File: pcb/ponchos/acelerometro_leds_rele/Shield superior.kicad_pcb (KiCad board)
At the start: 2 copper layers, 55 x 57 mm, 13 parts, among them J1 CONN_01X08, J2 CONN_01X06, J3 CONN_01X10, J4 CONN_01X08, J5 CONN_01X03, J6 Screw_Terminal_1x03, J7 CONN_01X08, K1 AZ850-x, Q1 BC548, U1 7805

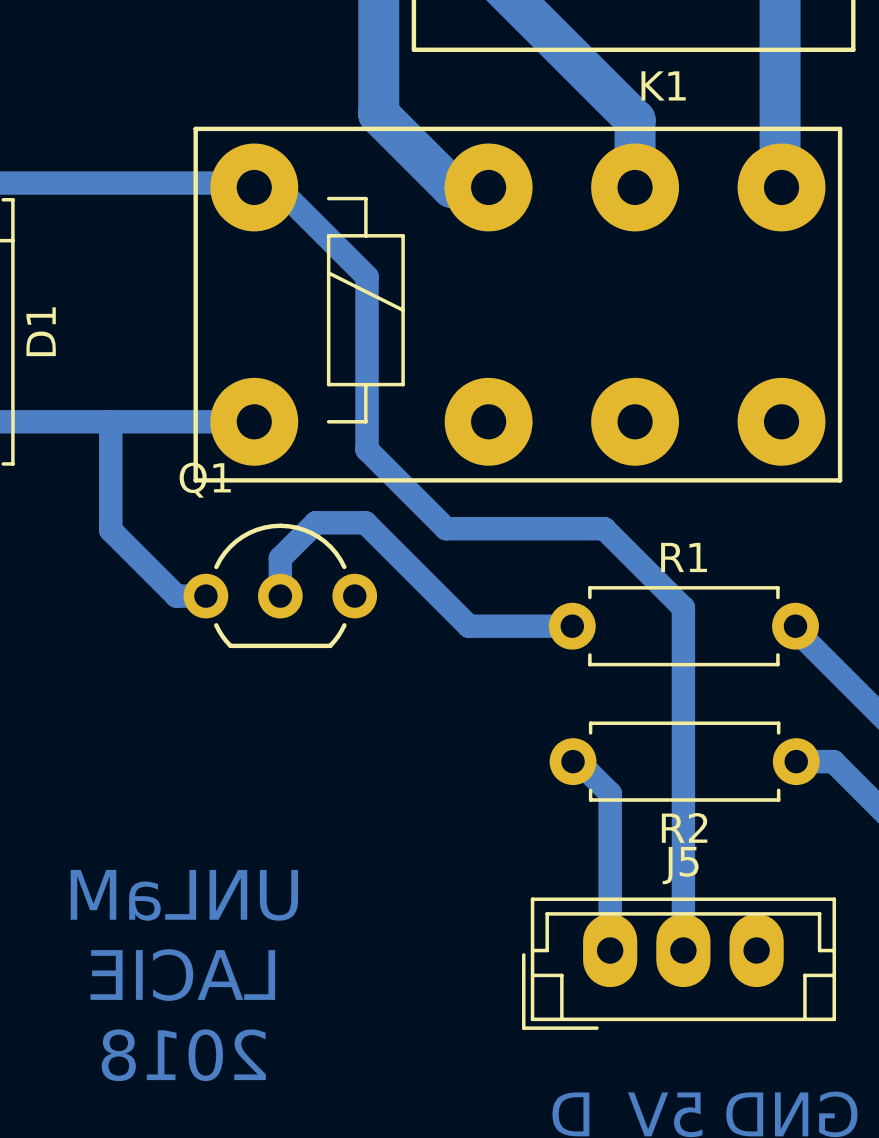
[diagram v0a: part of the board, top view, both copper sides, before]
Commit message: Pads mas grandes para el transistor.
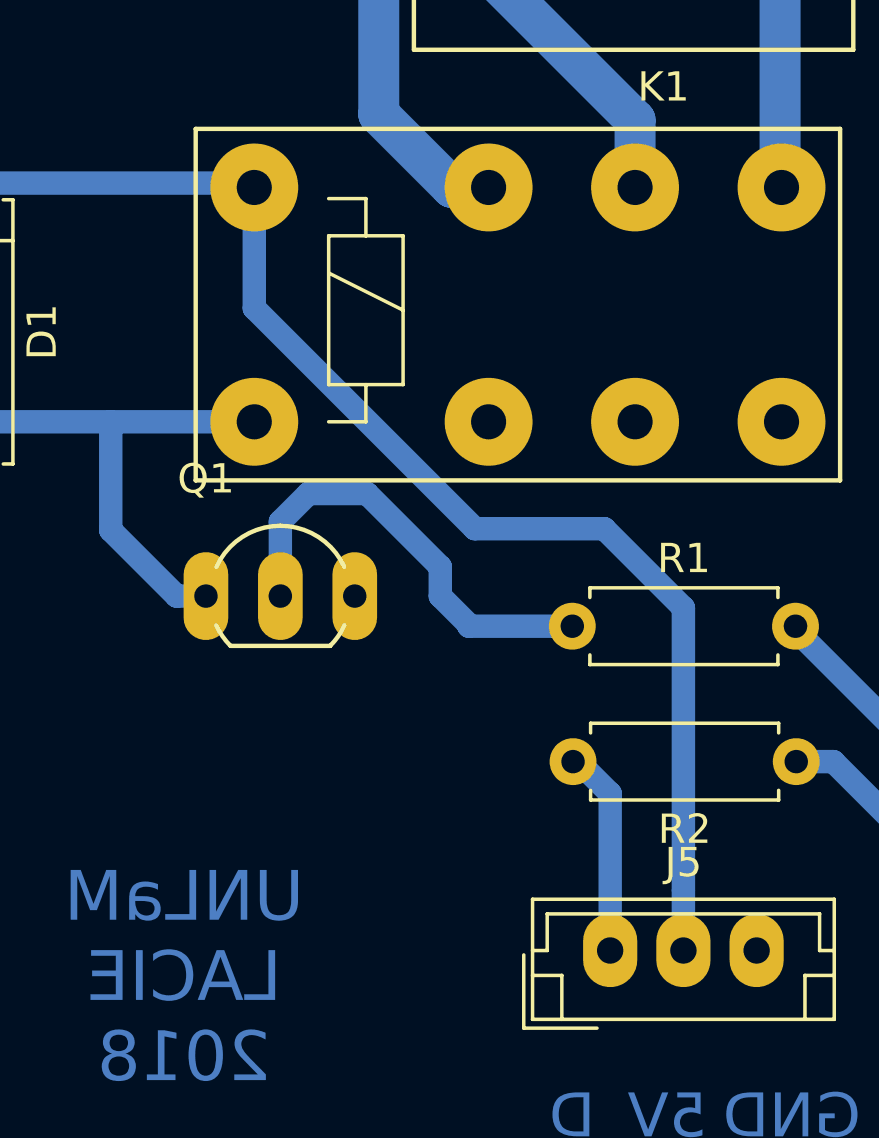
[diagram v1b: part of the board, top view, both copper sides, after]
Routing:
- net Net-(Q1-Pad2): track 13.2 -> 16.7 mm
- net +5V: track 82.6 -> 81.5 mm
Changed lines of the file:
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@@
     (links 21)
     (no_connects 0)
-    (area 20.424999 20.924999 75.575001 78.075001)
+    (area 8.22143 12.8 77.260001 79.900001)
     (thickness 1.6)
     (drawings 12)
-    (tracks 78)
+    (tracks 81)
     (zones 0)
     (modules 13)
@@
   )
   (setup
-    (last_trace_width 0.25)
+    (last_trace_width 0.8)
     (user_trace_width 0.6)
     (user_trace_width 0.8)
@@
     (mod_text_size 1 1)
     (mod_text_width 0.15)
-    (pad_size 1.85 1.85)
+    (pad_size 3 1.524)
     (pad_drill 0.8)
     (pad_to_mask_clearance 0.2)
@@
     (fp_line (start -1 -2.65) (end 6.1 -2.65) (layer F.CrtYd) (width 0.05))
     (fp_line (start 6.1 1.95) (end 6.1 -2.65) (layer F.CrtYd) (width 0.05))
-    (pad 2 thru_hole circle (at 2.54 0 90) (size 1.524 1.524) (drill 0.8) (layers *.Cu *.Mask F.SilkS)
+    (pad 2 thru_hole oval (at 2.54 0 90) (size 3 1.524) (drill 0.8) (layers *.Cu *.Mask F.SilkS)
       (net 42 "Net-(Q1-Pad2)"))
-    (pad 3 thru_hole circle (at 5.08 0 90) (size 1.524 1.524) (drill 0.8) (layers *.Cu *.Mask F.SilkS)
+    (pad 3 thru_hole oval (at 5.08 0 90) (size 3 1.524) (drill 0.8) (layers *.Cu *.Mask F.SilkS)
       (net 9 GND))
-    (pad 1 thru_hole circle (at 0 0 90) (size 1.524 1.524) (drill 0.8) (layers *.Cu *.Mask F.SilkS)
+    (pad 1 thru_hole oval (at 0 0 90) (size 3 1.524) (drill 0.8) (layers *.Cu *.Mask F.SilkS)
       (net 2 "Net-(D1-Pad2)"))
     (model TO_SOT_Packages_THT.3dshapes/TO-92_Inline_Wide.wrl
@@
   (gr_line (start 72.4408 74.6252) (end 72.4408 74.5236) (angle 90) (layer B.Paste) (width 0.2))
   (gr_line (start 23.9268 74.6252) (end 72.4408 74.6252) (angle 90) (layer B.Paste) (width 0.2))
+  (segment (start 59.8 50.4) (end 59.8 60.05) (width 0.8) (layer B.Cu) (net 1))
+  (segment (start 59.8 60.05) (end 59.8 62.1) (width 0.8) (layer B.Cu) (net 1))
+  (segment (start 52.679914 47.7) (end 57.1 47.7) (width 0.8) (layer B.Cu) (net 1))
+  (segment (start 57.1 47.7) (end 59.8 50.4) (width 0.8) (layer B.Cu) (net 1))
+  (segment (start 45.15 40.170086) (end 52.679914 47.7) (width 0.8) (layer B.Cu) (net 1))
+  (segment (start 45.15 36.05) (end 45.15 40.170086) (width 0.8) (layer B.Cu) (net 1))
   (segment (start 27.9 35.9) (end 24.75 32.75) (width 0.8) (layer B.Cu) (net 1))
   (segment (start 35 35.9) (end 27.9 35.9) (width 0.8) (layer B.Cu) (net 1))
@@
   (segment (start 35 39.3712) (end 35 35.9) (width 0.8) (layer B.Cu) (net 1))
   (segment (start 29.718 44.6532) (end 35 39.3712) (width 0.8) (layer B.Cu) (net 1))
-  (segment (start 45.15 36.05) (end 45.95 36.05) (width 0.8) (layer B.Cu) (net 1))
-  (segment (start 45.95 36.05) (end 49 39.1) (width 0.8) (layer B.Cu) (net 1))
-  (segment (start 59.8 50.4) (end 59.8 62.1) (width 0.8) (layer B.Cu) (net 1))
-  (segment (start 49 39.1) (end 49 45) (width 0.8) (layer B.Cu) (net 1))
   (segment (start 35 35.9) (end 45 35.9) (width 0.8) (layer B.Cu) (net 1))
   (segment (start 45 35.9) (end 45.15 36.05) (width 0.8) (layer B.Cu) (net 1))
-  (segment (start 49 45) (end 51.7 47.7) (width 0.8) (layer B.Cu) (net 1))
-  (segment (start 57.1 47.7) (end 59.8 50.4) (width 0.8) (layer B.Cu) (net 1))
-  (segment (start 51.7 47.7) (end 57.1 47.7) (width 0.8) (layer B.Cu) (net 1))
   (segment (start 43.5 50) (end 42.5 50) (width 0.8) (layer B.Cu) (net 2))
   (segment (start 40.25 47.75) (end 40.25 44.05) (width 0.8) (layer B.Cu) (net 2))
@@
   (segment (start 56.1 22.6) (end 58.1 24.6) (width 1.4) (layer B.Cu) (net 38))
   (segment (start 58.1 24.6) (end 58.1 26.15) (width 1.4) (layer B.Cu) (net 38))
-  (segment (start 48.9458 47.498) (end 47.252 47.498) (width 0.8) (layer B.Cu) (net 42))
-  (segment (start 48.9458 47.498) (end 52.4764 51.0286) (width 0.8) (layer B.Cu) (net 42))
+  (segment (start 47 46.5) (end 46.04 47.46) (width 0.8) (layer B.Cu) (net 42))
+  (segment (start 46.04 47.46) (end 46.04 50) (width 0.8) (layer B.Cu) (net 42))
+  (segment (start 49 46.5) (end 47 46.5) (width 0.8) (layer B.Cu) (net 42))
+  (segment (start 51.5 49) (end 49 46.5) (width 0.8) (layer B.Cu) (net 42))
+  (segment (start 51.5 50) (end 51.5 49) (width 0.8) (layer B.Cu) (net 42))
+  (segment (start 52.4764 50.9764) (end 51.5 50) (width 0.8) (layer B.Cu) (net 42))
+  (segment (start 52.4764 51.0286) (end 52.4764 50.9764) (width 0.8) (layer B.Cu) (net 42))
   (segment (start 56.007 51.0286) (end 52.4764 51.0286) (width 0.8) (layer B.Cu) (net 42))
   (segment (start 46.04 48.71) (end 46.04 50) (width 0.8) (layer B.Cu) (net 42))
-  (segment (start 47.252 47.498) (end 46.04 48.71) (width 0.8) (layer B.Cu) (net 42))
   (zone (net 9) (net_name GND) (layer B.Cu) (hatch edge 0.508)
     (connect_pads (clearance 0.8))
